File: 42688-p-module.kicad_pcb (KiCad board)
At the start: 2 copper layers, 13.2 x 18 mm, 12 parts, among them IC1 ICM-42688-P, J1 Conn_01x06_Pin, J2 Conn_01x01_Pin, X1 O3232768151850

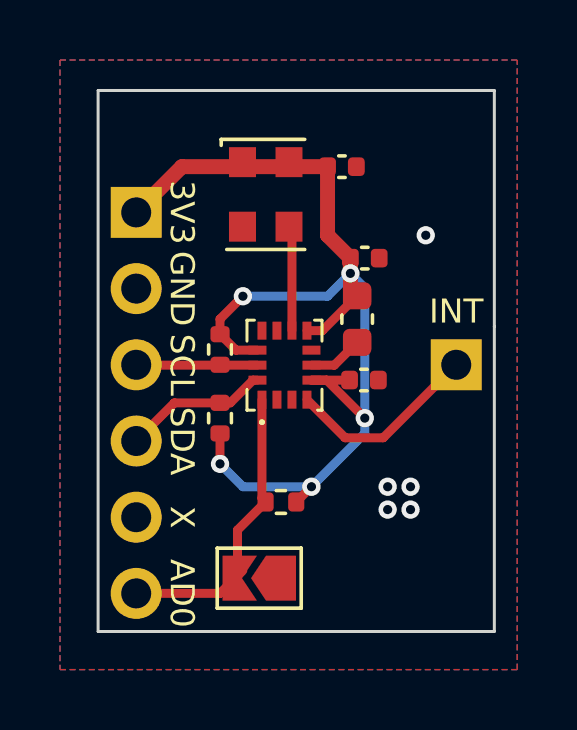
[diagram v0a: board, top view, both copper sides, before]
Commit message: support SPI
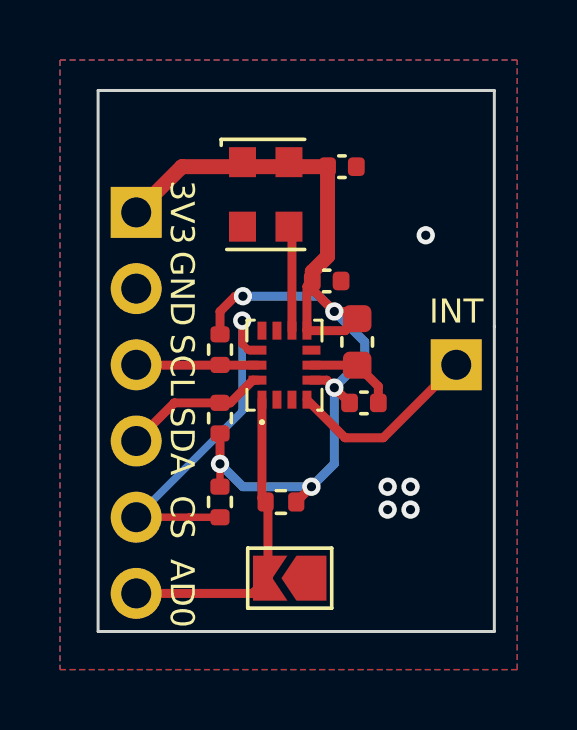
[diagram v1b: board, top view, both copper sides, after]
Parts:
- added R4: 3.9k, Resistor_SMD:R_0402_1005Metric, F.Cu at (109.5, 93.5)
- moved C2 1.48 mm to (113.0, 86.1)
- moved JP1 1.02 mm to (111.8, 96.0)
- moved C1 0.76 mm to (114.3, 90.2)
- moved C3 0.76 mm to (114.0, 88.1)
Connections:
- IC1 pad 12: +3.3V -> /CS
- J1 pad 5: unconnected-(J1-Pin_5-Pad5) -> /CS
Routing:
- net /CS: track 0.00 -> 12.2 mm, vias 0 -> 1
- net +3.3V: track 37.5 -> 36.2 mm
- net GND: track 1.84 -> 3.07 mm
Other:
- board text added: "CS"
- board text removed: "X"
